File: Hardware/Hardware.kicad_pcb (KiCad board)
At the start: 4 copper layers, 52 parts, among them J1 Conn_01x04, J2 Conn_Coaxial, J3 USB_C_Receptacle_USB2.0_16P, J4 Conn_01x04, Q1 MMBT2222A, SW1 SW_Push, U1 STM32WB55RGVx, U2 USBLC6-2SC6, U3 MIC5365-3.3YD5, U4 BME280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

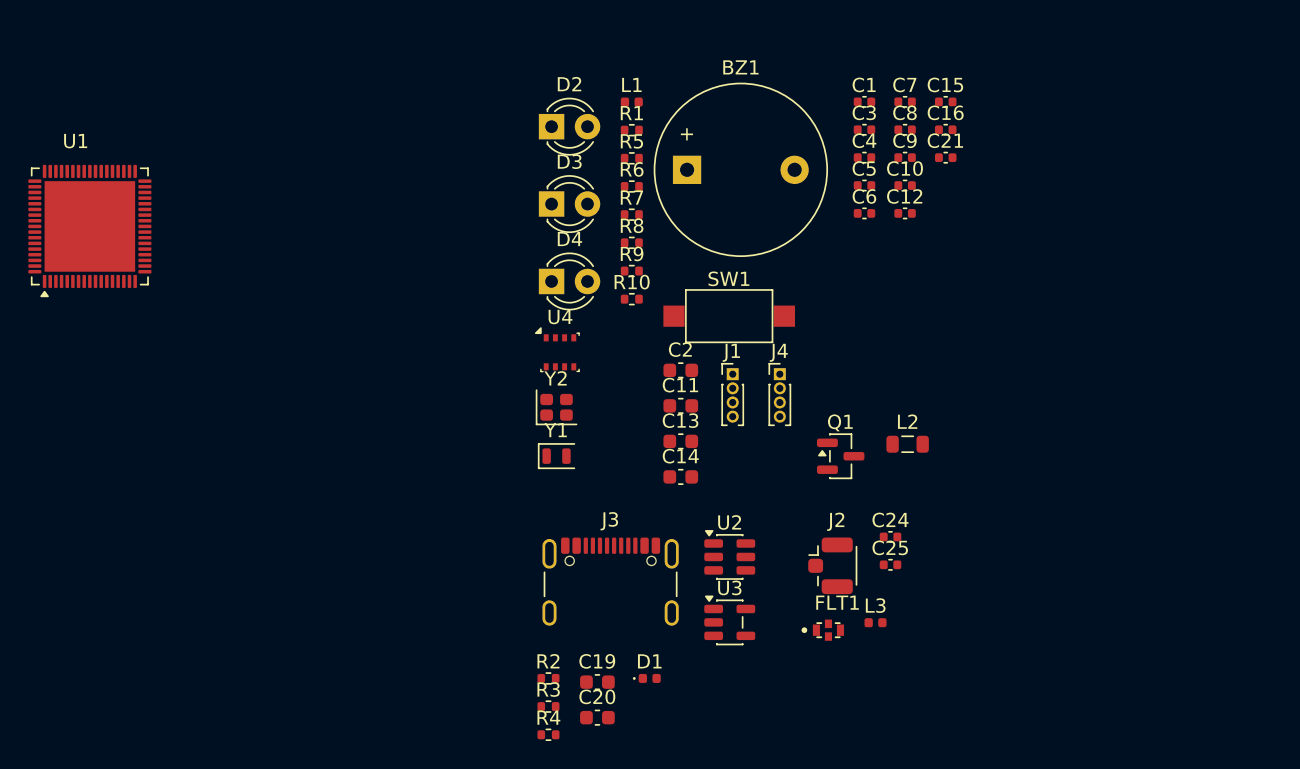
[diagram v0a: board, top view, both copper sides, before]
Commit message: [PLACEMENT DES COMPOSANT ET DIMENSIONNEMENT] : Avant de désigner le type de signal à chaque couche et commencer le routage, j'ai d'abord commencer par organiser les composants selon la schématique et comment j'aimerais avoir le produit finale
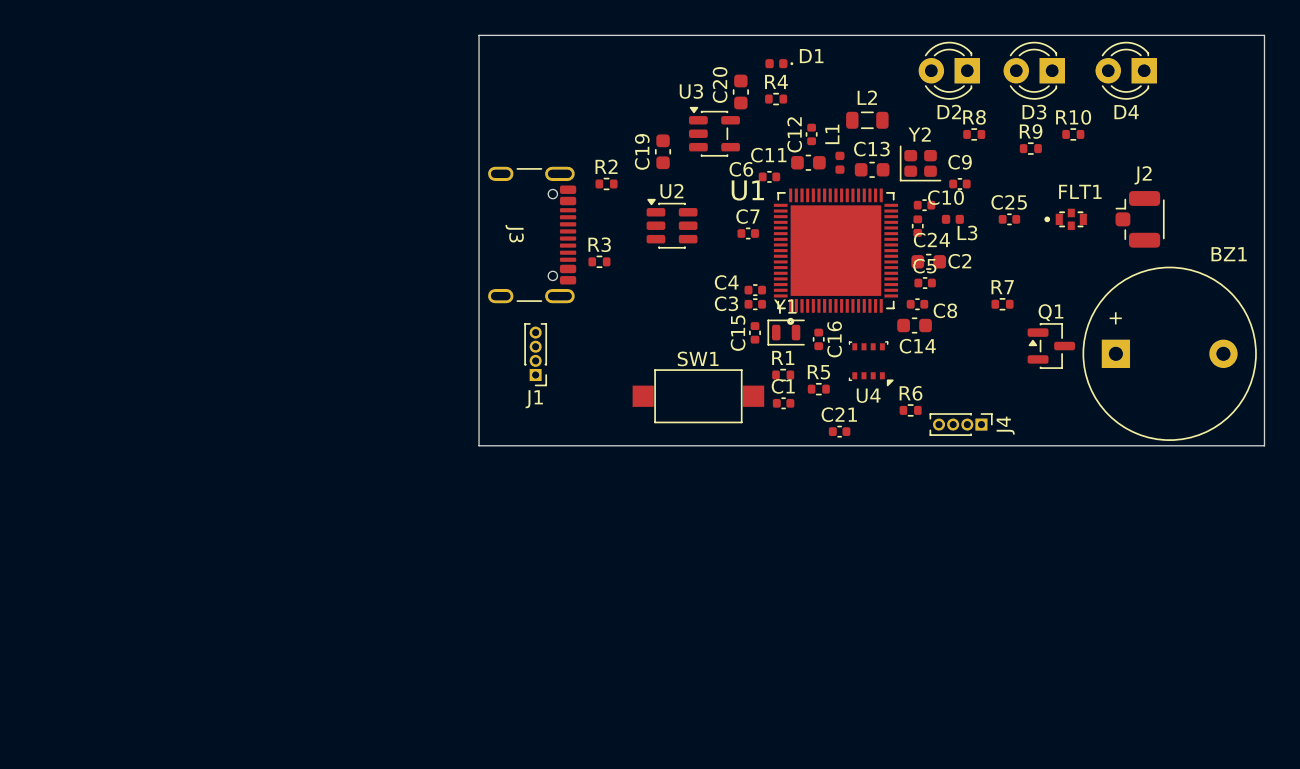
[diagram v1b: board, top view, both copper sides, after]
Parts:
- U1: footprint Package_DFN_QFN:QFN-68-1EP_8x8mm_P0.4mm_EP6.4x6.4mm -> my_personnal_Library_footprint:QFN40P800X800X100-69N
- moved U1 52.7 mm to (154.7, 71.7)
- moved R4 47.7 mm to (150.5, 61.0)
- moved C20 45.4 mm to (148.0, 60.5), turned to 90 degrees
- moved D4 44.4 mm to (176.5, 59.0), turned to 180 degrees
- moved D1 44.4 mm to (150.5, 58.5), turned to 180 degrees
- moved C19 37.8 mm to (142.5, 64.7), turned to 90 degrees
- moved D3 36.6 mm to (170.0, 59.0), turned to 180 degrees
- moved R2 35.2 mm to (138.5, 67.0)
- moved U3 34.5 mm to (146.1, 63.5)
- moved FLT1 33.7 mm to (171.3, 69.5)
- moved R10 33.3 mm to (171.5, 63.5)
- moved BZ1 33.0 mm to (174.5, 79.0)
- moved J2 32.7 mm to (176.1, 69.5)
- moved R3 31.6 mm to (138.0, 72.5)
- moved Y2 31.0 mm to (160.7, 65.5)
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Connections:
- net Net-(J3-D+-PadA6) renamed /USB SCHEME/D+
- net Net-(J3-D--PadA7) renamed /USB SCHEME/D-
- C1 pad 1: unconnected-(C1-Pad1) -> /RESET
- C25 pad 1: Net-(FLT1-IN) -> /RF
- FLT1 pad 1: Net-(FLT1-IN) -> /RF
- FLT1 pad 3: Net-(FLT1-OUT) -> /RF
- J2 pad 1: Net-(FLT1-OUT) -> /RF
- L3 pad 2: Net-(FLT1-IN) -> /RF
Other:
- board outline added: 55.5 x 29 mm
- rule pad_to_mask_clearance: 0.08 -> 0

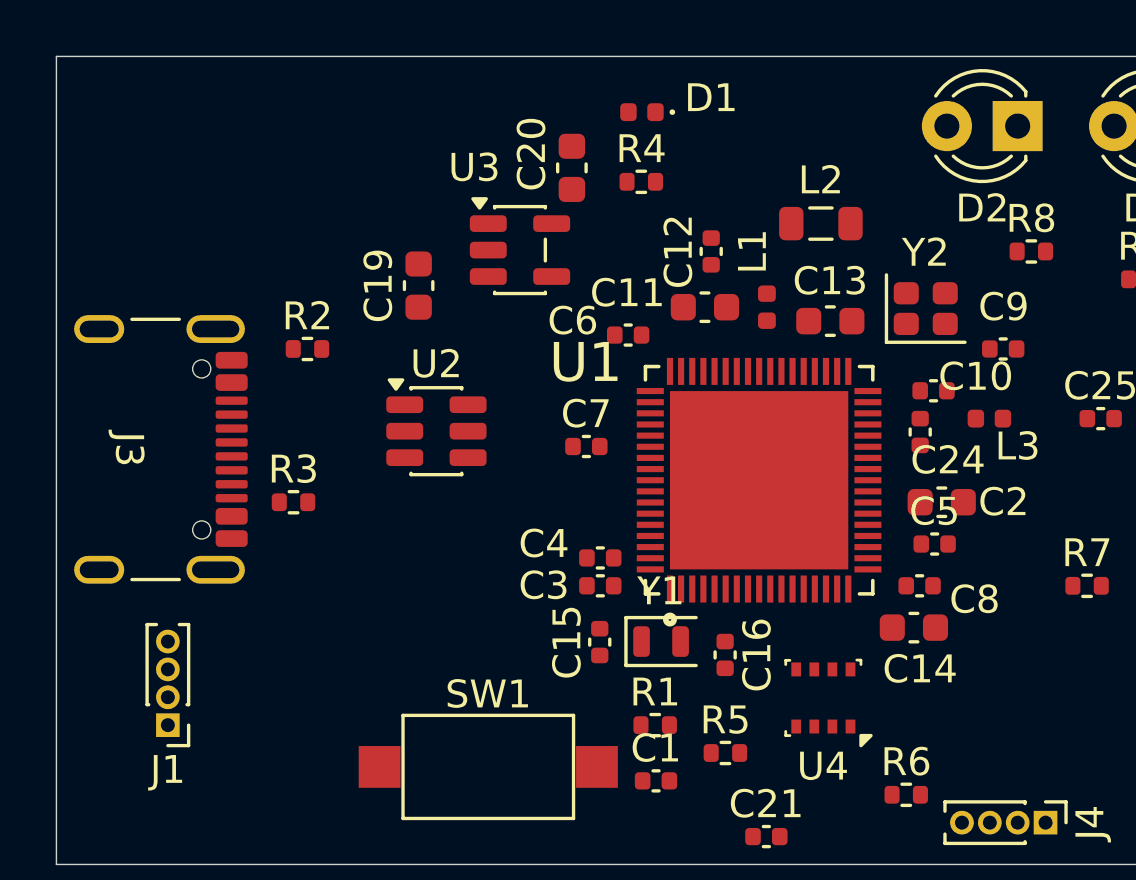
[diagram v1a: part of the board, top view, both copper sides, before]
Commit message: [CORRECTION DES ERREURS SOLDER MASK] : Correction et attribution des valeurs de solder mask avec les valeurs correct de PCB Way
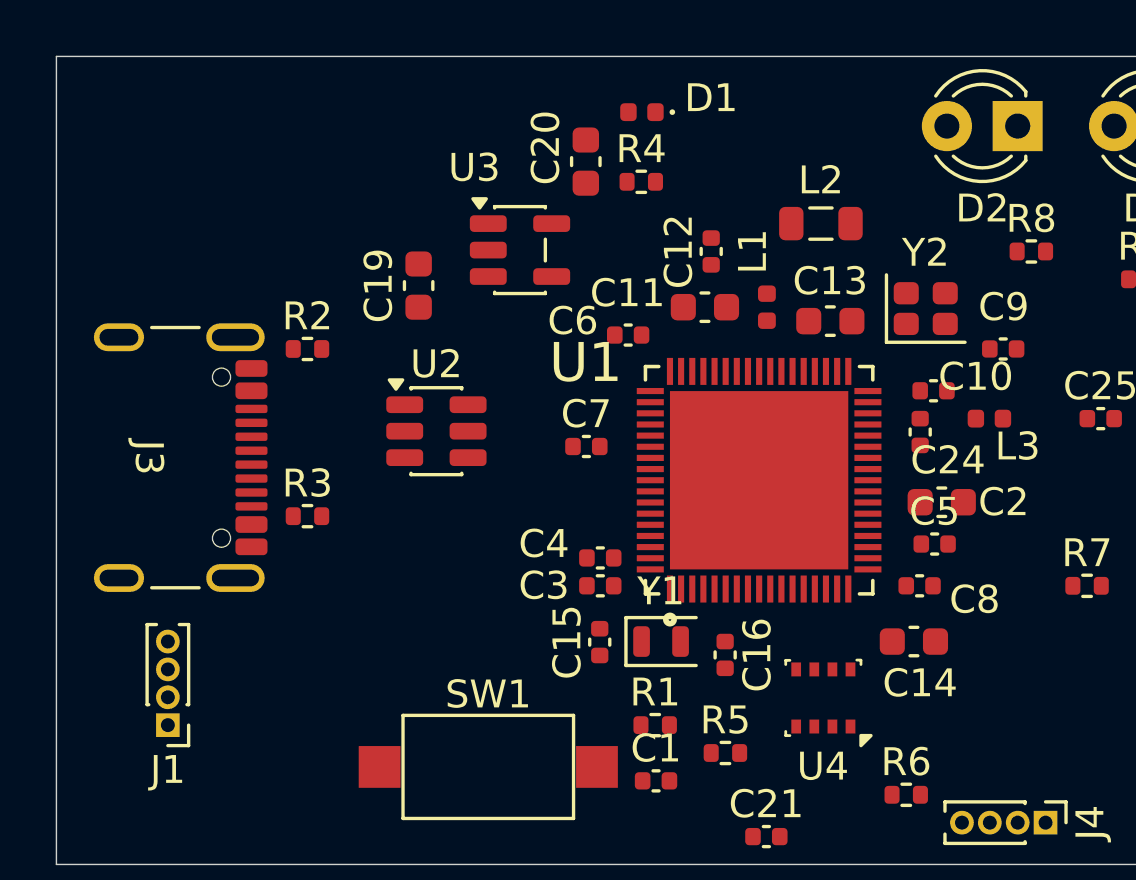
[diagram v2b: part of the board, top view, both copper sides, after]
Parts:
- moved J3 0.77 mm to (132.8, 70.9)
- moved R3 0.71 mm to (138.5, 73.0)
- moved C20 0.55 mm to (148.5, 60.3)
- moved C14 0.50 mm to (160.3, 77.5)
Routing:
- added copper zone on In2.Cu, net +3V3
- added copper zone on In1.Cu, net GND
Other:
- rule pad_to_mask_clearance: 0 -> 0.05
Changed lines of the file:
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@@
 			(dielectric_constraints yes)
 		)
-		(pad_to_mask_clearance 0)
-		(solder_mask_min_width 0.125)
-		(pad_to_paste_clearance -0.02)
+		(pad_to_mask_clearance 0.05)
+		(pad_to_paste_clearance 0.02)
 		(allow_soldermask_bridges_in_footprints no)
 		(tenting front back)
@@
 	(footprint "Connector_USB:USB_C_Receptacle_GCT_USB4105-xx-A_16P_TopMnt_Horizontal"
 		(layer "F.Cu")
-		(at 132.11 70.605 -90)
+		(at 132.82 70.9 -90)
 		(descr "USB 2.0 Type C Receptacle, GCT, 16P, top mounted, horizontal, 5A: https://gct.co/files/drawings/usb4105.pdf")
 		(tags "USB C Type-C Receptacle SMD USB 2.0 16P 16C USB4105-15-A USB4105-15-A-060 USB4105-15-A-120 USB4105-GF-A USB4105-GF-A-060 USB4105-GF-A-120")
@@
 	(footprint "Capacitor_SMD:C_0603_1608Metric"
 		(layer "F.Cu")
-		(at 148 60.5 90)
+		(at 148.5 60.275 90)
 		(descr "Capacitor SMD 0603 (1608 Metric), square (rectangular) end terminal, IPC-7351 nominal, (Body size source: IPC-SM-782 page 76, https://www.pcb-3d.com/wordpress/wp-content/uploads/ipc-sm-782a_amendment_1_and_2.pdf), generated with kicad-footprint-generator")
 		(tags "capacitor")
@@
 		(sheetname "/")
 		(sheetfile "Hardware.kicad_sch")
-		(attr smd)
+		(solder_mask_margin 0.1)
+		(clearance 0.05)
+		(attr smd allow_soldermask_bridges)
 		(fp_line
 			(start 4.08 -4.08)
@@
 	(footprint "Capacitor_SMD:C_0603_1608Metric"
 		(layer "F.Cu")
-		(at 160.275 77 180)
+		(at 160.275 77.5 180)
 		(descr "Capacitor SMD 0603 (1608 Metric), square (rectangular) end terminal, IPC-7351 nominal, (Body size source: IPC-SM-782 page 76, https://www.pcb-3d.com/wordpress/wp-content/uploads/ipc-sm-782a_amendment_1_and_2.pdf), generated with kicad-footprint-generator")
 		(tags "capacitor")
@@
 	(footprint "Resistor_SMD:R_0402_1005Metric"
 		(layer "F.Cu")
-		(at 138.01 72.5)
+		(at 138.51 73)
 		(descr "Resistor SMD 0402 (1005 Metric), square (rectangular) end terminal, IPC-7351 nominal, (Body size source: IPC-SM-782 page 72, https://www.pcb-3d.com/wordpress/wp-content/uploads/ipc-sm-782a_amendment_1_and_2.pdf), generated with kicad-footprint-generator")
 		(tags "resistor")
@@
 		(sheetname "/RF SECTION/")
 		(sheetfile "RF.kicad_sch")
+		(solder_mask_margin 0)
+		(clearance 0)
 		(attr smd)
 		(fp_rect
@@
 			(pinfunction "Ext")
 			(pintype "passive")
+			(clearance 0)
 		)
 		(pad "2" smd roundrect
@@
 		(layer "Edge.Cuts")
 	)
+	(zone
+		(net 4)
+		(net_name "GND")
+		(layer "In1.Cu")
+		(hatch edge 0.5)
+		(connect_pads
+			(clearance 0.3)
+		)
+		(min_thickness 0.25)
+		(filled_areas_thickness no)
+		(fill yes
+			(thermal_gap 0.5)
+			(thermal_bridge_width 0.5)
+		)
+		(polygon
+			(pts
+				(xy 129 55.5) (xy 129 77) (xy 129.5 87) (xy 185.5 86) (xy 185.5 56)
+			)
+		)
+	)
+	(zone
+		(net 1)
+		(net_name "+3V3")
+		(layer "In2.Cu")
+		(hatch edge 0.5)
+		(priority 1)
+		(connect_pads
+			(clearance 0.3)
+		)
+		(min_thickness 0.25)
+		(filled_areas_thickness no)
+		(fill yes
+			(thermal_gap 0.5)
+			(thermal_bridge_width 0.5)
+		)
+		(polygon
+			(pts
+				(xy 128.5 55.5) (xy 128.5 86) (xy 186.5 86) (xy 186 55.5)
+			)
+		)
+	)
 	(embedded_fonts no)

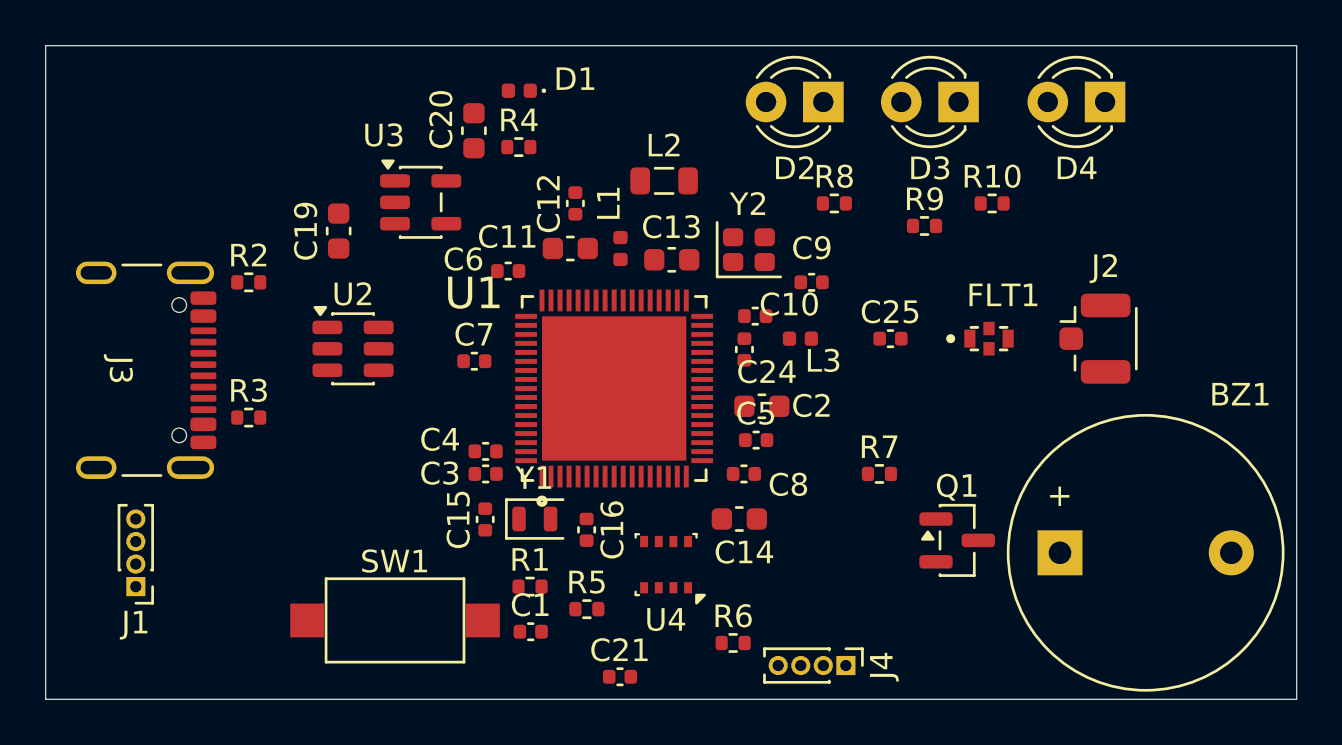
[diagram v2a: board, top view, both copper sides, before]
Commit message: [ROUTAGE ET CONTROL DRC] : J'ai routé la carte sur 4 couches. F.cu layer : c'est la prémière couche In1.cu layer: c'est le plan de masse In2.cu layer : c'est le plan de tension 3.3V B.cu layer : c'est pour les signaux qui passent par des via.
J'ai routé le PCB ensuite,j'ai effectué le Test DRC, puis j'ai corrigé
les bug manifeste.
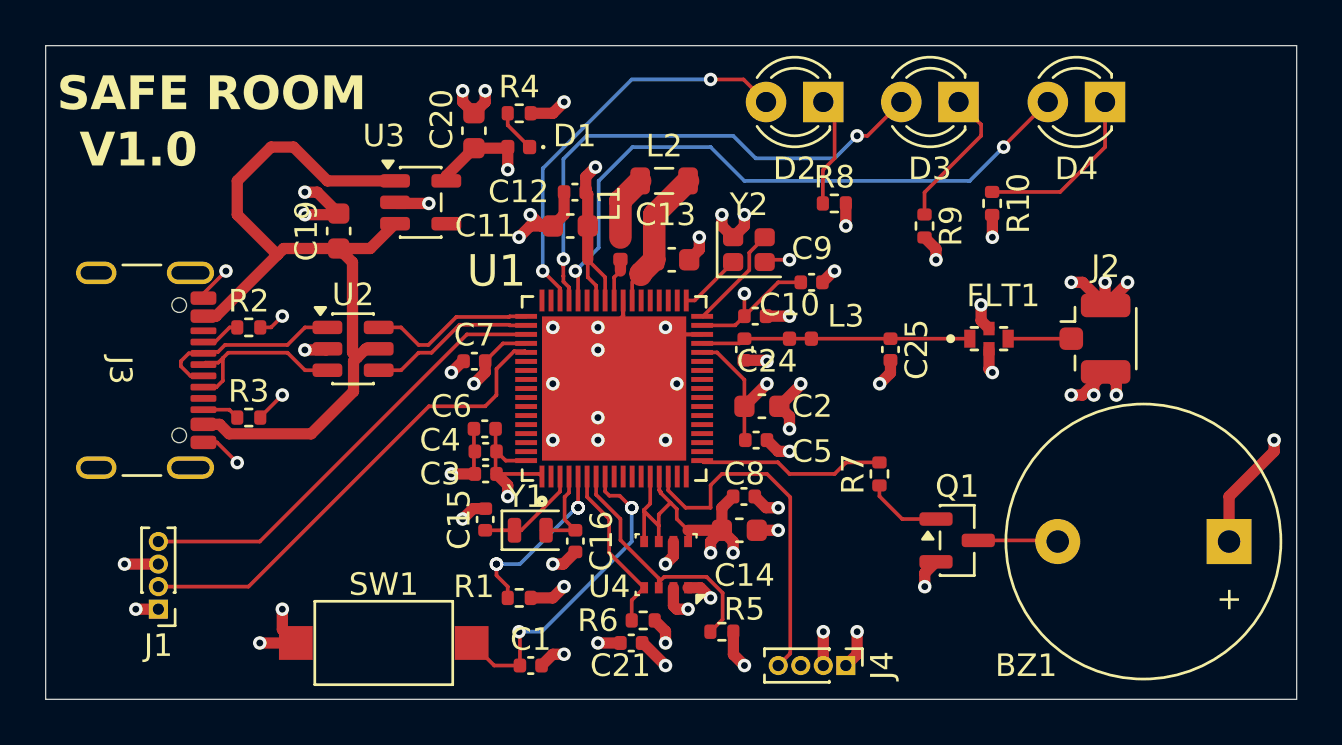
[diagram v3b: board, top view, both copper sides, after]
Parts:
- moved BZ1 7.52 mm to (182.0, 78.5), turned to 180 degrees
- moved C6 7.08 mm to (149.0, 73.5)
- moved R5 6.07 mm to (159.5, 82.5)
- moved R6 4.11 mm to (156.0, 82.0)
- moved D1 2.50 mm to (150.5, 61.0)
- moved R2 2.00 mm to (138.5, 69.0)
- moved C21 1.58 mm to (155.5, 83.0)
- moved R4 1.50 mm to (150.5, 59.5)
- moved C1 1.50 mm to (151.0, 84.0)
- moved J1 1.41 mm to (134.5, 81.5)
- moved SW1 1.12 mm to (144.5, 83.0)
- moved C11 1.00 mm to (152.8, 64.5)
- moved C8 1.00 mm to (160.5, 76.5)
- moved C16 0.71 mm to (153.0, 78.5)
- moved R1 0.69 mm to (150.5, 81.0)
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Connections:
- FLT1 pad 3: /RF -> Net-(FLT1-OUT)
- J2 pad 1: /RF -> Net-(FLT1-OUT)
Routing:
- net GND: track 0.00 -> 74.3 mm, vias 0 -> 61
- net +3V3: track 0.00 -> 64.0 mm, vias 0 -> 15
- net +5V: track 0.00 -> 37.9 mm
- net /HOT_YELLOW: track 0.00 -> 28.4 mm, vias 0 -> 2
- net /ORANGE_GOOD: track 0.00 -> 23.2 mm, vias 0 -> 2
- net /SWDCLK: track 0.00 -> 21.3 mm
- net /SWDIO: track 0.00 -> 20.1 mm
- net /COLD_BLUE: track 0.00 -> 18.2 mm, vias 0 -> 2
- net /MQ2_sensor: track 0.00 -> 15.7 mm
- net /RESET: track 0.00 -> 14.4 mm, vias 0 -> 3
- net /RF: track 0.00 -> 12.0 mm
- net /I2C_SDA: track 0.00 -> 11.5 mm
- net /USB SCHEME/D-: track 0.00 -> 8.52 mm
- net Net-(U1-PA3): track 0.00 -> 8.32 mm
- net /USB SCHEME/D+: track 0.00 -> 8.02 mm
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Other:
- board text added: "SAFE ROOM"
- board text added: "V1.0"

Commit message: [ANNOTATION DU DESIGN]: Annotation des module present sur la carte
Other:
- board text added: "BME280"
- board text added: "DESIGNER PAR KAMDA TEZEBO"
- board text added: "RESET"
- board text added: "RF"
- board text added: "ST-LINK"
- board text added: "USB-C"
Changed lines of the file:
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@@
 		(tags "capacitor")
 		(property "Reference" "C21"
-			(at -0.48 1 0)
+			(at -0.98 1.5 0)
 			(layer "F.SilkS")
 			(effects
@@
 		(layer "Edge.Cuts")
 	)
+	(gr_text "RESET"
+		(at 138.5 84.5 0)
+		(layer "F.SilkS")
+		(effects
+			(font
+				(size 0.5 0.5)
+				(thickness 0.125)
+				(bold yes)
+			)
+			(justify left bottom)
+		)
+	)
+	(gr_text "RF"
+		(at 178.5 67 0)
+		(layer "F.SilkS")
+		(effects
+			(font
+				(size 1 1)
+				(thickness 0.25)
+				(bold yes)
+			)
+			(justify left bottom)
+		)
+	)
 	(gr_text "V1.0"
 		(at 131 62 0)
@@
 		)
 	)
+	(gr_text "BME280"
+		(at 157.5 85 0)
+		(layer "F.SilkS")
+		(effects
+			(font
+				(size 0.5 0.5)
+				(thickness 0.125)
+				(bold yes)
+			)
+			(justify left bottom)
+		)
+	)
+	(gr_text "USB-C"
+		(at 129.5 65.5 0)
+		(layer "F.SilkS")
+		(effects
+			(font
+				(size 1 1)
+				(thickness 0.25)
+				(bold yes)
+			)
+			(justify left bottom)
+		)
+	)
 	(gr_text "SAFE ROOM"
 		(at 130 59.5 0)
@@
 		)
 	)
+	(gr_text "ST-LINK"
+		(at 132.5 84 90)
+		(layer "F.SilkS")
+		(effects
+			(font
+				(size 1 1)
+				(thickness 0.25)
+				(bold yes)
+			)
+			(justify left bottom)
+		)
+	)
+	(gr_text "DESIGNER PAR\nKAMDA TEZEBO"
+		(at 181 77 0)
+		(layer "B.SilkS")
+		(effects
+			(font
+				(size 1.5 1.5)
+				(thickness 0.3)
+				(bold yes)
+			)
+			(justify left bottom mirror)
+		)
+	)

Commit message: [PREPARATION DES FICHIERS DE COMMANDES] : Generation de fichier de placement et de fichier gebers. J'ai généré le fichier de placement des composants selon l'origine de la grille. J'ai également généré le fichier geber qui contient les plans de fabrications de notre carte PCB.
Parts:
- R10, R4, R8, R9: value 330 -> 220
